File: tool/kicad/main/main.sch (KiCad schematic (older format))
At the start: 146 parts, among them J1 MICRO-USB-AB, K1 CONN_3, K2 CONN_3, P1 TEST_POINT, P10 TEST_POINT, P11 TEST_POINT, P12 TEST_POINT, P13 TEST_POINT, P14 TEST_POINT, P15 TEST_POINT, P16 TEST_POINT, P17 TEST_POINT, P18 TEST_POINT, P19 TEST_POINT, P2 TEST_POINT, P20 TEST_POINT, P21 TEST_POINT, P22 TEST_POINT, P23 TEST_POINT, P24 TEST_POINT, P25 TEST_POINT, P26 TEST_POINT, P27 TEST_POINT, P28 TEST_POINT, P29 TEST_POINT, P3 TEST_POINT, P30 CONN_3X2, P31 CONN_2, P32 CONN_2, P33 TEST_POINT, P34 TEST_POINT, P35 CONN_6, P37 TEST_POINT, P38 TEST_POINT, P4 TEST_POINT, P5 MIDI-IN, P6 TEST_POINT, P7 TEST_POINT, P8 TEST_POINT, P9 TEST_POINT, U1 SN74LVC2T45, U2 ST-USBLC6-2, U3 EFM32GG332, U4 YM2413, U5 LM386, U6 LM386, U7 ACPL-M21L, X1 48Mhz, X2 CRYSTAL

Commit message: cleanup schematic
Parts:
- removed C13, C14, C22, C23: 10uF, symbol C
- removed C18, C19: 2.2nF, symbol C
- removed C20, C21: 1uF, symbol C
- removed D12: D, symbol D
- removed K2: CONN_3, symbol CONN_3
- removed P31, P32: CONN_2, symbol CONN_2
- removed P33, P34: TEST_POINT, symbol TEST_POINT
- removed P5: MIDI-IN, symbol CONN_5
- removed R15: 220, symbol R
- removed R37, R39: 10k, symbol R
- removed R40, R41, R45, R46, R47, R50, R51, R52: 2k2, symbol R
- removed R43, R44: 4k7/NC, symbol R
- removed R48, R49: 100, symbol R
- removed R53, R54: 1k, symbol R
- removed U5, U6: LM386, symbol LM386
- removed U7: ACPL-M21L, symbol ACPL-M21L
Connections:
- net labels removed: MOA, MOA2, MOA3, MOI, MOI2, ROA, ROA2, ROA3, ROI, ROI2
- wire segments 355 -> 267
- no-connect marks 17 -> 14

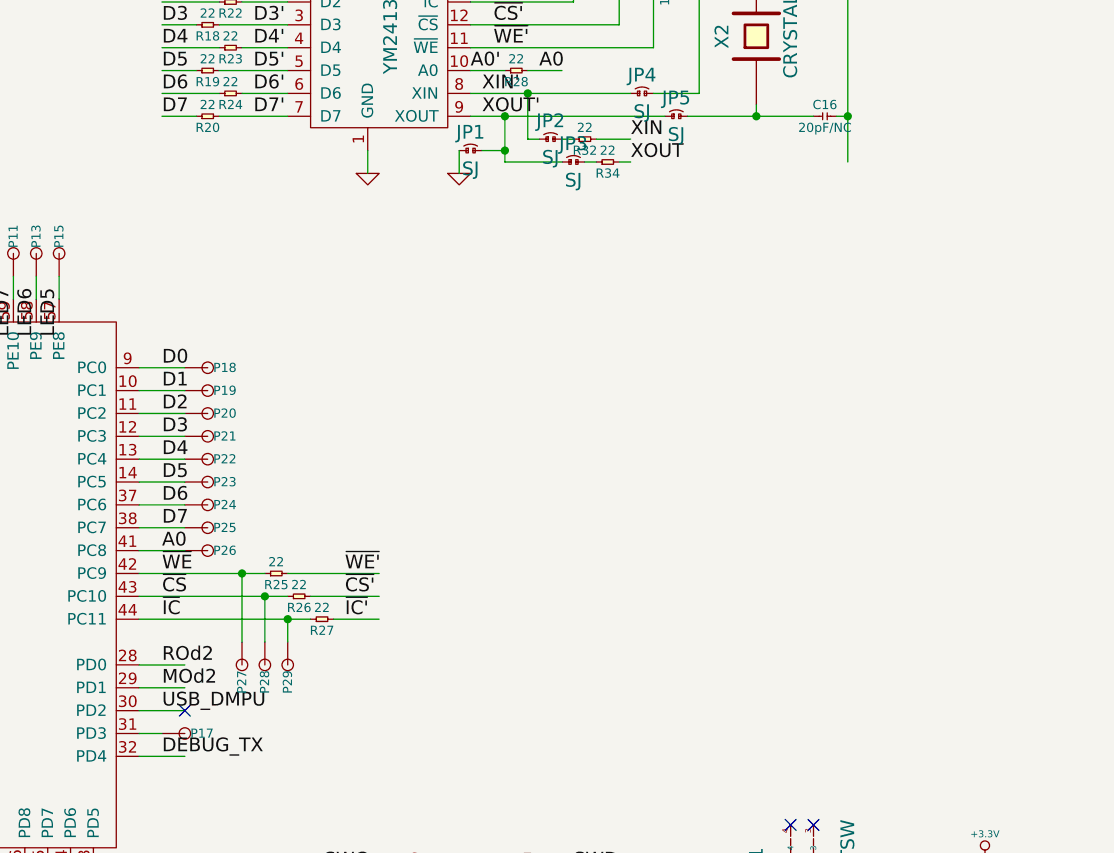
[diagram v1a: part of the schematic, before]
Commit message: adapt audio to don't have the 2k2s on this board by default
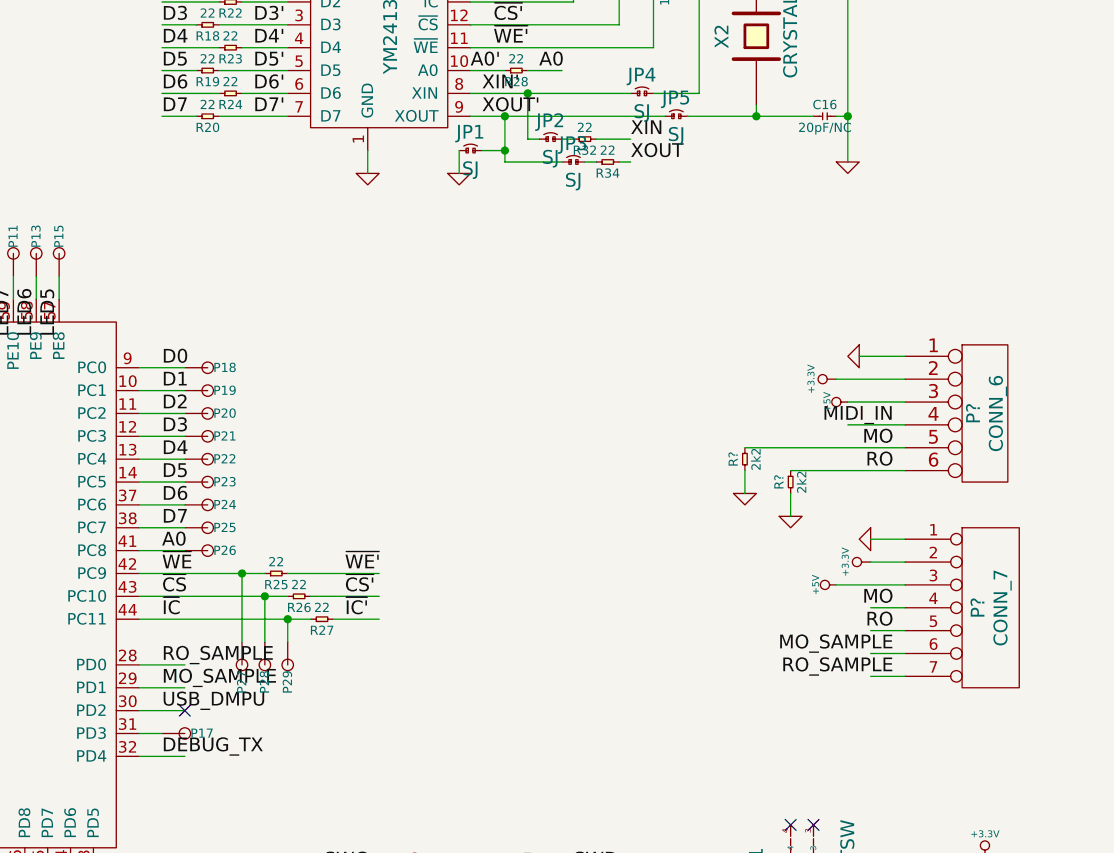
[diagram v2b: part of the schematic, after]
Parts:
- added P?: CONN_6, symbol CONN_6
- added P?: CONN_7, symbol CONN_7
- added R? (x2): 2k2, symbol R
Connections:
- net labels added: MO_SAMPLE, RO_SAMPLE
- net labels removed: MOd2, ROd2
- wire segments 267 -> 282
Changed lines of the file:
@@
 	5300 4800 5100 4800
 Text Label 5200 4700 0    60   ~ 0
-ROd2
+RO_SAMPLE
 Text Label 5200 4800 0    60   ~ 0
-MOd2
+MO_SAMPLE
 Wire Wire Line
 	5300 4900 5100 4900
@@
 Wire Wire Line
 	4050 6750 4050 5600
+$Comp
+L CONN_6 P?
+U 1 1 53C2A362
+P 8800 3600
+F 0 "P?" V 8750 3600 60  0000 C CNN
+F 1 "CONN_6" V 8850 3600 60  0000 C CNN
+F 2 "" H 8800 3600 60  0000 C CNN
+F 3 "" H 8800 3600 60  0000 C CNN
+	1    8800 3600
+	1    0    0    -1
+$EndComp
+$Comp
+L GND #PWR?
+U 1 1 53C2A556
+P 8250 3350
+F 0 "#PWR?" H 8250 3350 30  0001 C CNN
+F 1 "GND" H 8250 3280 30  0001 C CNN
+F 2 "" H 8250 3350 60  0000 C CNN
+F 3 "" H 8250 3350 60  0000 C CNN
+	1    8250 3350
+	0    1    1    0
+$EndComp
+$Comp
+L +3.3V #PWR?
+U 1 1 53C2A8E1
+P 8150 3450
+F 0 "#PWR?" H 8150 3410 30  0001 C CNN
+F 1 "+3.3V" H 8150 3560 30  0000 C CNN
+F 2 "" H 8150 3450 60  0000 C CNN
+F 3 "" H 8150 3450 60  0000 C CNN
+	1    8150 3450
+	0    -1   -1   0
+$EndComp
+$Comp
+L +5V #PWR?
+U 1 1 53C2ABFC
+P 8200 3550
+F 0 "#PWR?" H 8200 3640 20  0001 C CNN
+F 1 "+5V" H 8200 3640 30  0000 C CNN
+F 2 "" H 8200 3550 60  0000 C CNN
+F 3 "" H 8200 3550 60  0000 C CNN
+	1    8200 3550
+	0    -1   -1   0
+$EndComp
+Wire Wire Line
+	8250 3350 8450 3350
+Wire Wire Line
+	8150 3450 8450 3450
+Wire Wire Line
+	8200 3550 8450 3550
+Wire Wire Line
+	8200 3650 8450 3650
+Wire Wire Line
+	7750 3750 8450 3750
+Wire Wire Line
+	7950 3850 8450 3850
+Text Label 8400 3650 2    60   ~ 0
+MIDI_IN
+Text Label 8400 3750 2    60   ~ 0
+MO
+Text Label 8400 3850 2    60   ~ 0
+RO
+$Comp
+L GND #PWR?
+U 1 1 53C2BDCF
+P 8300 4150
+F 0 "#PWR?" H 8300 4150 30  0001 C CNN
+F 1 "GND" H 8300 4080 30  0001 C CNN
+F 2 "" H 8300 4150 60  0000 C CNN
+F 3 "" H 8300 4150 60  0000 C CNN
+	1    8300 4150
+	0    1    1    0
+$EndComp
+$Comp
+L +3.3V #PWR?
+U 1 1 53C2BE4B
+P 8300 4250
+F 0 "#PWR?" H 8300 4210 30  0001 C CNN
+F 1 "+3.3V" H 8300 4360 30  0000 C CNN
+F 2 "" H 8300 4250 60  0000 C CNN
+F 3 "" H 8300 4250 60  0000 C CNN
+	1    8300 4250
+	0    -1   -1   0
+$EndComp
+Wire Wire Line
+	8300 4150 8450 4150
+Wire Wire Line
+	8300 4250 8450 4250
+$Comp
+L R R?
+U 1 1 53C2AB64
+P 7950 3900
+F 0 "R?" H 7950 3950 40  0000 C CNN
+F 1 "2k2" H 7950 3850 40  0000 C CNN
+F 2 "" H 7950 3900 60  0000 C CNN
+F 3 "" H 7950 3900 60  0000 C CNN
+	1    7950 3900
+	0    -1   -1   0
+$EndComp
+$Comp
+L R R?
+U 1 1 53C2AF20
+P 7750 3800
+F 0 "R?" H 7750 3850 40  0000 C CNN
+F 1 "2k2" H 7750 3750 40  0000 C CNN
+F 2 "" H 7750 3800 60  0000 C CNN
+F 3 "" H 7750 3800 60  0000 C CNN
+	1    7750 3800
+	0    -1   -1   0
+$EndComp
+$Comp
+L GND #PWR?
+U 1 1 53C2B31F
+P 7750 3950
+F 0 "#PWR?" H 7750 3950 30  0001 C CNN
+F 1 "GND" H 7750 3880 30  0001 C CNN
+F 2 "" H 7750 3950 60  0000 C CNN
+F 3 "" H 7750 3950 60  0000 C CNN
+	1    7750 3950
+	1    0    0    -1
+$EndComp
+Wire Wire Line
+	7750 3850 7750 3950
+$Comp
+L GND #PWR?
+U 1 1 53C2B556
+P 7950 4050
+F 0 "#PWR?" H 7950 4050 30  0001 C CNN
+F 1 "GND" H 7950 3980 30  0001 C CNN
+F 2 "" H 7950 4050 60  0000 C CNN
+F 3 "" H 7950 4050 60  0000 C CNN
+	1    7950 4050
+	1    0    0    -1
+$EndComp
+Wire Wire Line
+	7950 3950 7950 4050
+$Comp
+L GND #PWR?
+U 1 1 53C2BE1A
+P 8200 2500
+F 0 "#PWR?" H 8200 2500 30  0001 C CNN
+F 1 "GND" H 8200 2430 30  0001 C CNN
+F 2 "" H 8200 2500 60  0000 C CNN
+F 3 "" H 8200 2500 60  0000 C CNN
+	1    8200 2500
+	1    0    0    -1
+$EndComp
+$Comp
+L CONN_7 P?
+U 1 1 53C2AB8E
+P 8800 4450
+F 0 "P?" V 8770 4450 60  0000 C CNN
+F 1 "CONN_7" V 8870 4450 60  0000 C CNN
+F 2 "" H 8800 4450 60  0000 C CNN
+F 3 "" H 8800 4450 60  0000 C CNN
+	1    8800 4450
+	1    0    0    -1
+$EndComp
+$Comp
+L +5V #PWR?
+U 1 1 53C2AEE8
+P 8150 4350
+F 0 "#PWR?" H 8150 4440 20  0001 C CNN
+F 1 "+5V" H 8150 4440 30  0000 C CNN
+F 2 "" H 8150 4350 60  0000 C CNN
+F 3 "" H 8150 4350 60  0000 C CNN
+	1    8150 4350
+	0    -1   -1   0
+$EndComp
+Wire Wire Line
+	8150 4350 8450 4350
+Wire Wire Line
+	8300 4450 8450 4450
+Wire Wire Line
+	8300 4550 8450 4550
+Text Label 8400 4450 2    60   ~ 0
+MO
+Text Label 8400 4550 2    60   ~ 0
+RO
+Wire Wire Line
+	8300 4650 8450 4650
+Wire Wire Line
+	8300 4750 8450 4750
+Text Label 8400 4650 2    60   ~ 0
+MO_SAMPLE
+Text Label 8400 4750 2    60   ~ 0
+RO_SAMPLE
 $EndSCHEMATC

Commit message: annotation
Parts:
- gave numbers to parts that had none: 4

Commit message: main board WIP
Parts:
- removed P1, P11, P12, P13, P14, P15, P16, P17, P18, P19, P2, P20, P21, P22, P23, P24, P25, P26, P3, P4, P6, P7, P8, P9: TEST_POINT, symbol TEST_POINT
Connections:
- wire segments 282 -> 275
- no-connect marks 14 -> 19

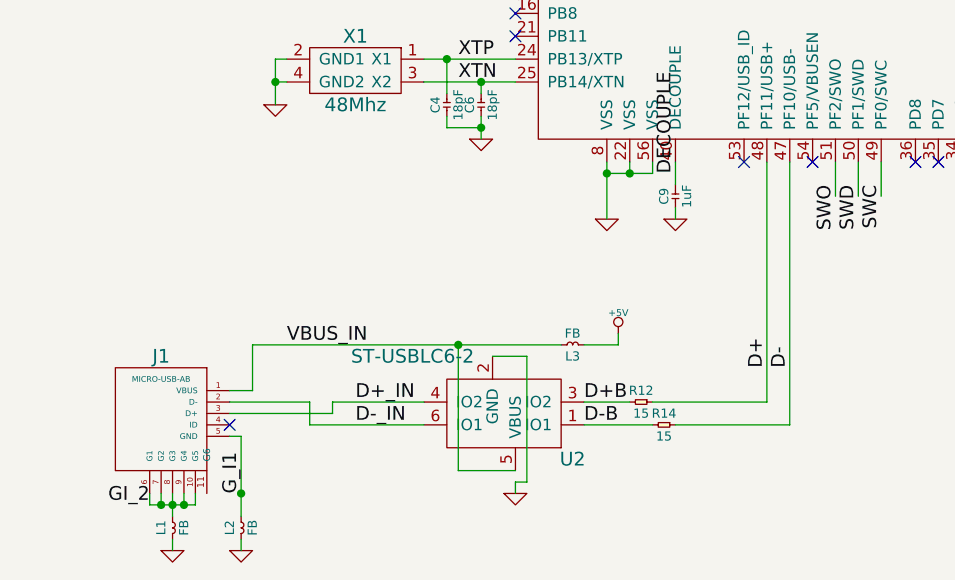
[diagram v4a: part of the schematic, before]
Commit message: fix main USB connector
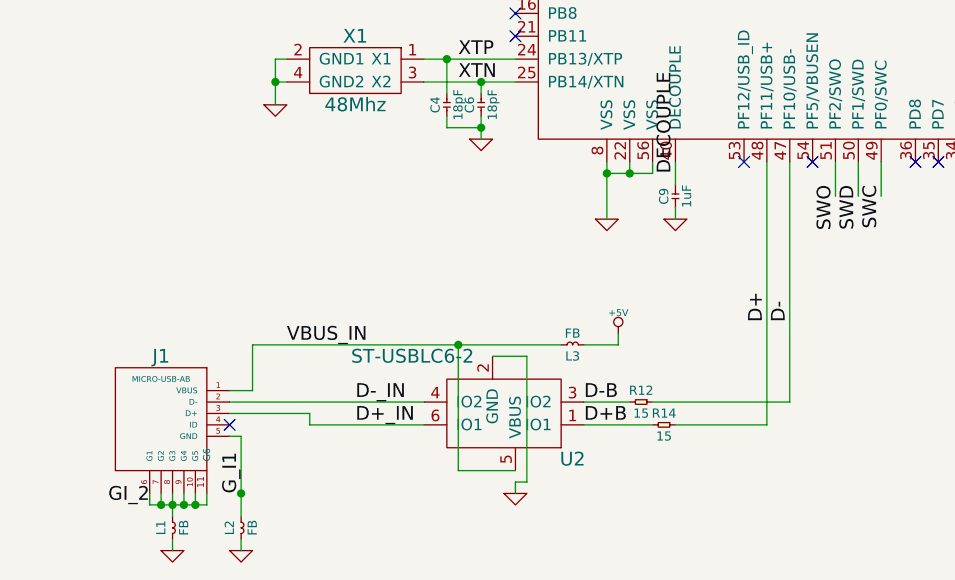
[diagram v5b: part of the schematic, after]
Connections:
- wire segments 275 -> 274
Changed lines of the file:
@@
 	1    0    0    -1
 $EndComp
-Text Label 4050 6500 1    60   ~ 0
+Text Label 4050 6300 1    60   ~ 0
 D-
-Text Label 3950 6500 1    60   ~ 0
+Text Label 3950 6300 1    60   ~ 0
 D+
 $Comp
@@
 Text Label 1850 6400 0    60   ~ 0
 VBUS_IN
+Text Label 2150 6650 0    60   ~ 0
+D-_IN
 Text Label 2150 6750 0    60   ~ 0
-D-_IN
-Text Label 2150 6650 0    60   ~ 0
 D+_IN
 Text Label 1650 7050 1    60   ~ 0
@@
 	1    0    0    -1
 $EndComp
+Text Label 3150 6650 0    60   ~ 0
+D-B
 Text Label 3150 6750 0    60   ~ 0
-D-B
-Text Label 3150 6650 0    60   ~ 0
 D+B
 $Comp
@@
 	1250 7050 1250 7100
 Wire Wire Line
-	1250 7100 1450 7100
+	1250 7100 1500 7100
 Connection ~ 1350 7100
 Wire Wire Line
@@
 	2850 7000 2850 7050
 Wire Wire Line
-	3550 6750 4050 6750
-Wire Wire Line
-	2450 6650 2050 6650
-Wire Wire Line
-	2050 6650 2050 6700
-Wire Wire Line
-	2050 6700 1600 6700
-Wire Wire Line
-	1600 6650 1950 6650
-Wire Wire Line
-	1950 6650 1950 6750
+	1600 6650 2450 6650
 Wire Wire Line
 	1950 6750 2450 6750
@@
 NoConn ~ 2850 5050
 Wire Wire Line
-	3450 6650 3950 6650
-Wire Wire Line
-	3950 6650 3950 5600
-Wire Wire Line
-	4050 6750 4050 5600
+	3450 6650 4050 6650
 $Comp
 L CONN_6 P5
@@
 NoConn ~ 5100 5000
 NoConn ~ 4050 3100
+Wire Wire Line
+	1950 6750 1950 6700
+Wire Wire Line
+	1950 6700 1600 6700
+Wire Wire Line
+	4050 6650 4050 5600
+Wire Wire Line
+	3950 5600 3950 6750
+Wire Wire Line
+	3950 6750 3550 6750
+Wire Wire Line
+	1500 7100 1500 7050
+Connection ~ 1450 7100
 $EndSCHEMATC
